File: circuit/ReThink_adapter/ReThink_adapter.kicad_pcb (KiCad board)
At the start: 2 copper layers, 82 x 52 mm, 76 parts, among them J1 FH34SRJ-34S-0.5SH(50), J2 FH34SRJ-6S-0.5SH(50), J3 Mezzanine, J4 XF3M(1)-3015-1B, J5 XF3M(1)-0815-1B, J6 FH34SRJ-40S-0.5SH(50), J7 FH52-40S-0.5SH, J8 XF3M(1)-1415-1B, U1 PCAL6416AHF, U2 LM2775DSG, U3 PCA9306, U4 TPS610333DRLR

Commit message: finish routing
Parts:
- removed TP1: P0_7, TestPoint:TestPoint_THTPad_D1.5mm_Drill0.7mm
- added J10: OUT2, Connector_PinHeader_2.54mm:PinHeader_1x02_P2.54mm_Vertical, F.Cu at (161.5, 78.0)
- added J11: OUT3, Connector_PinHeader_2.54mm:PinHeader_1x02_P2.54mm_Vertical, F.Cu at (116.5, 88.0)
- added J9: OUT1, Connector_PinHeader_2.54mm:PinHeader_1x02_P2.54mm_Vertical, F.Cu at (133.0, 82.5)
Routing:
- net GND: track 239.0 -> 341.0 mm, vias 323 -> 328
- net BL_5V: track 103.3 -> 107.9 mm
- net LED_3V3: track 142.9 -> 146.8 mm
- net /TP2_RST: track 28.1 -> 30.8 mm
- net /TP1_RST: track 65.9 -> 67.5 mm
- net /LEDMICMUTE: track 46.3 -> 47.6 mm
- net Net-(J6-Pin_12): track 79.8 -> 78.5 mm
- net Net-(J6-Pin_11): track 83.0 -> 81.9 mm
- net Net-(J6-Pin_13): track 77.0 -> 76.0 mm
- net Net-(J6-Pin_8): track 87.1 -> 86.1 mm
- net /DRV16: track 87.3 -> 86.4 mm
- net /HOTKEY: track 122.2 -> 121.4 mm
- net /LEDMUTE: track 64.0 -> 64.9 mm
- net Net-(J9-Pin_1): track 2.97 -> 3.79 mm
- net /DRV17: track 36.7 -> 36.0 mm
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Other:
- board text added: "BL5V"
- board text added: "GND"
- board text added: "LED3V3"
- board text added: "P07"
- board text added: "TODO: - Silkscreen/logos - BOM - Cable guide 3D print"

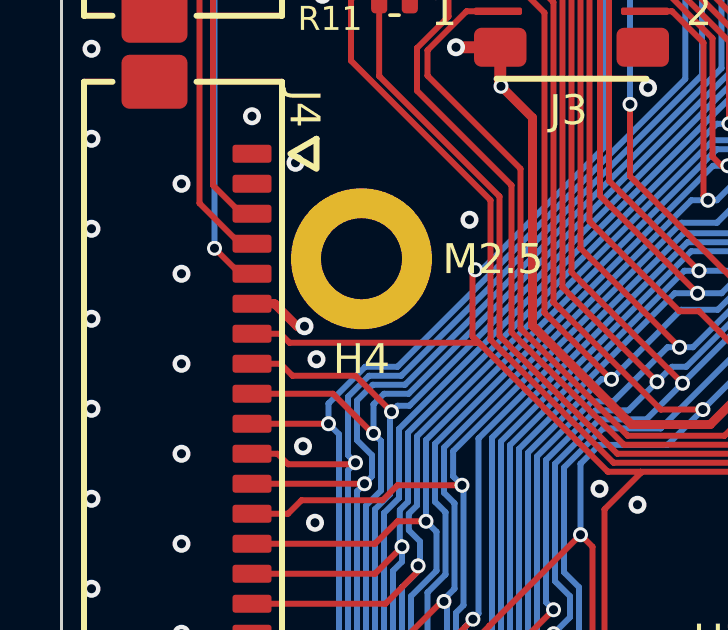
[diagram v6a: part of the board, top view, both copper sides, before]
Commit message: added BOM
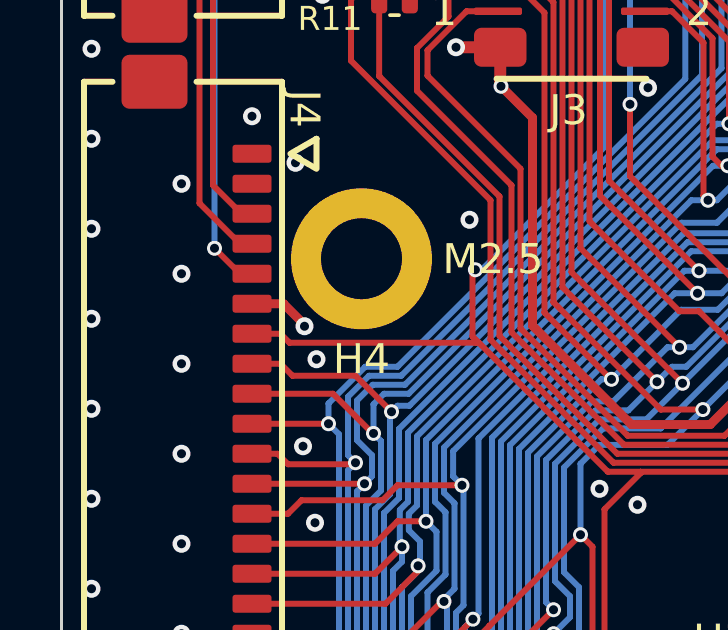
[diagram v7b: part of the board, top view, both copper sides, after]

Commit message: add step 3d model, update BOM
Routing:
- net GND: vias 328 -> 329
